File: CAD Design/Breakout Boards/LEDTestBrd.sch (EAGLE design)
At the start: 14 parts

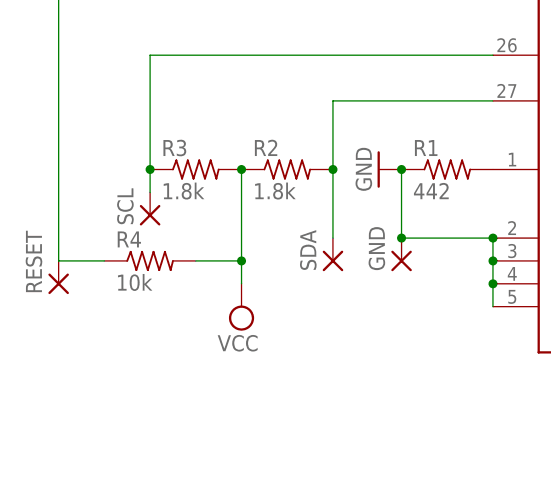
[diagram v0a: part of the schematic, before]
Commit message: First breakout board design review
Minor changes to silkscreens, added documentation.  Acc. and LED driver
boards ready for board house.
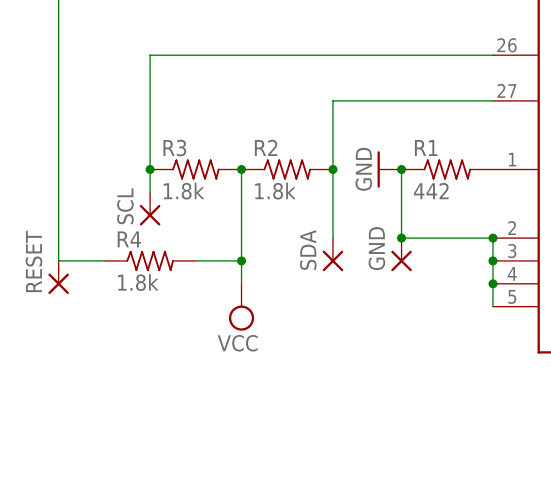
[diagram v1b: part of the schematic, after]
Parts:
- R4: value 10k -> 1.8k
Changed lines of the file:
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@@
 <part name="VCC" library="wirepad" deviceset="2,15/1,0" device=""/>
 <part name="GND" library="wirepad" deviceset="2,15/1,0" device=""/>
-<part name="R4" library="resistor" deviceset="R-US_" device="R0402" value="10k"/>
+<part name="R4" library="resistor" deviceset="R-US_" device="R0402" value="1.8k"/>
 </parts>
 <sheets>
